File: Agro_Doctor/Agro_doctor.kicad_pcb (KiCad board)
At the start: 2 copper layers, 49 parts, among them J1 Bluetooth, J10 M2, J11 M3, J12 Power_Motor, J13 MS_Conn, J2 Bluetooth, J3 3STEPPER,1SERVO, J4 Bluetooth, J5 Encoders, Stepper1, J6 3 MPU, HUMIDITY, PH, J7 Power_Logic, J8 M1, J9 M4, SW1 SW_DIP_x01, U1 Motor_Driver, U10 Boost, U2 A4988_1, U3 A4988_2, U4 A4988_3, U5 A4988_4, U6 L298_M2,3, U7 L298_M4, U8 Buck, U9 STM32F407_Discovery

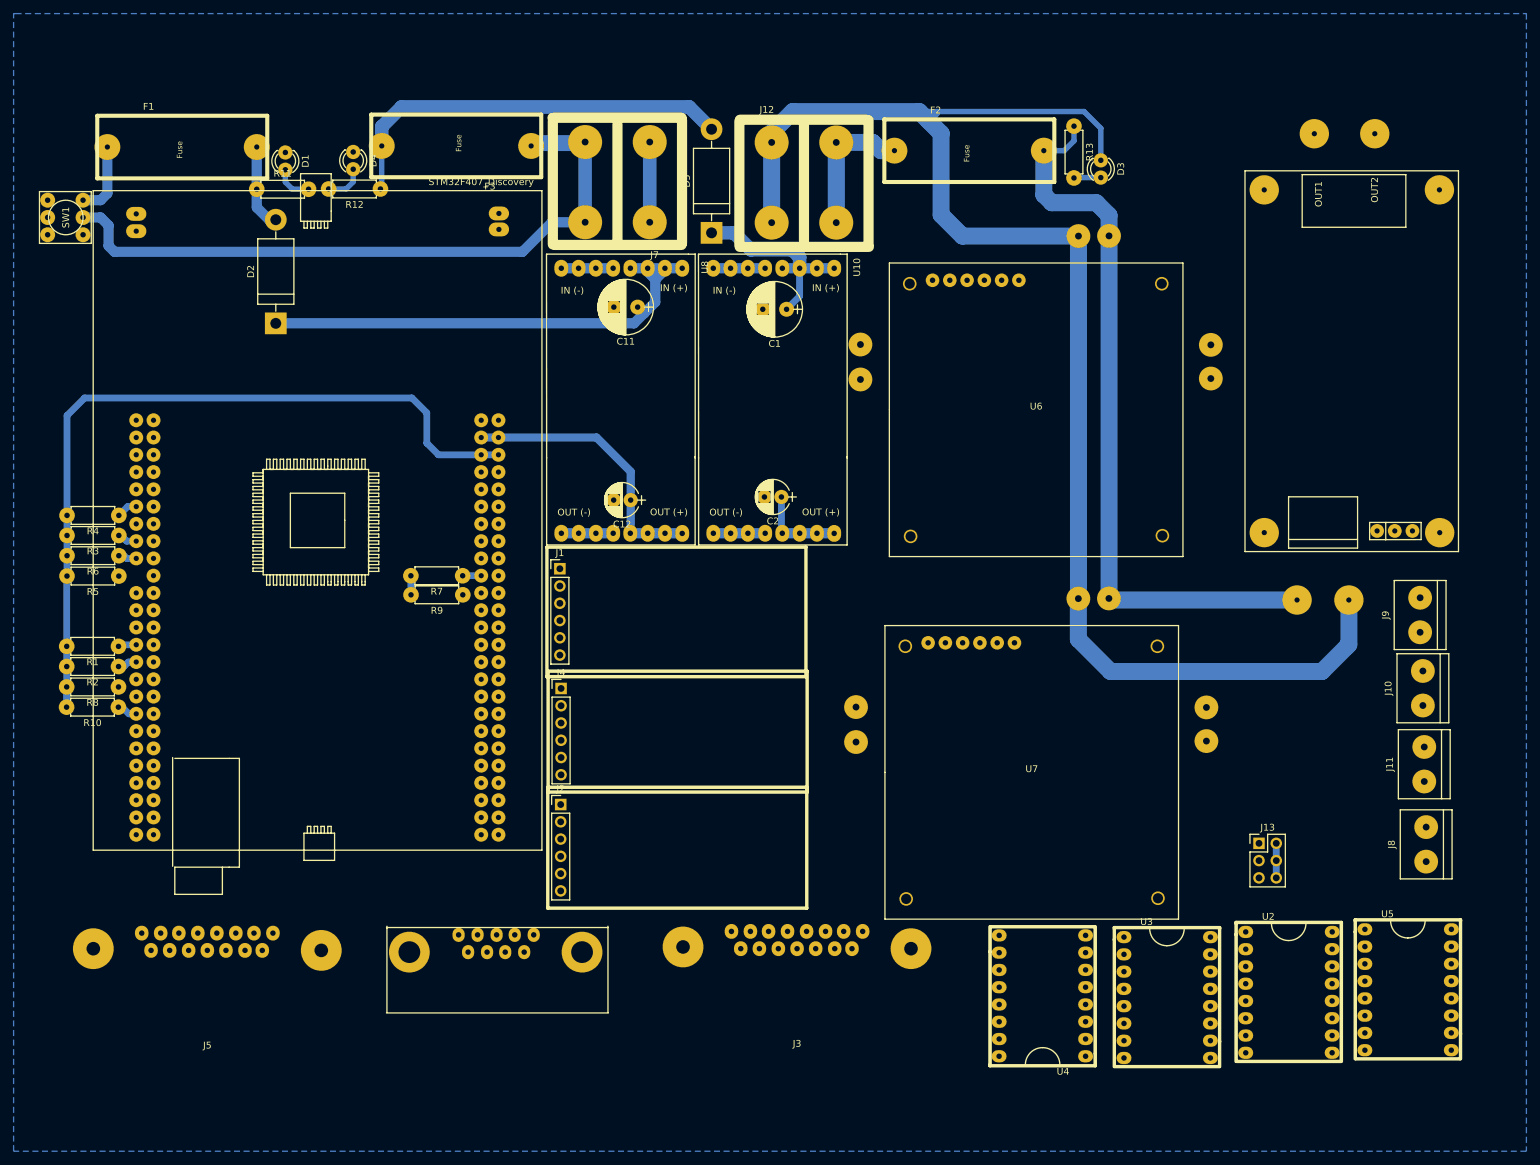
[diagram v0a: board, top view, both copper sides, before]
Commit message: added the minor project file
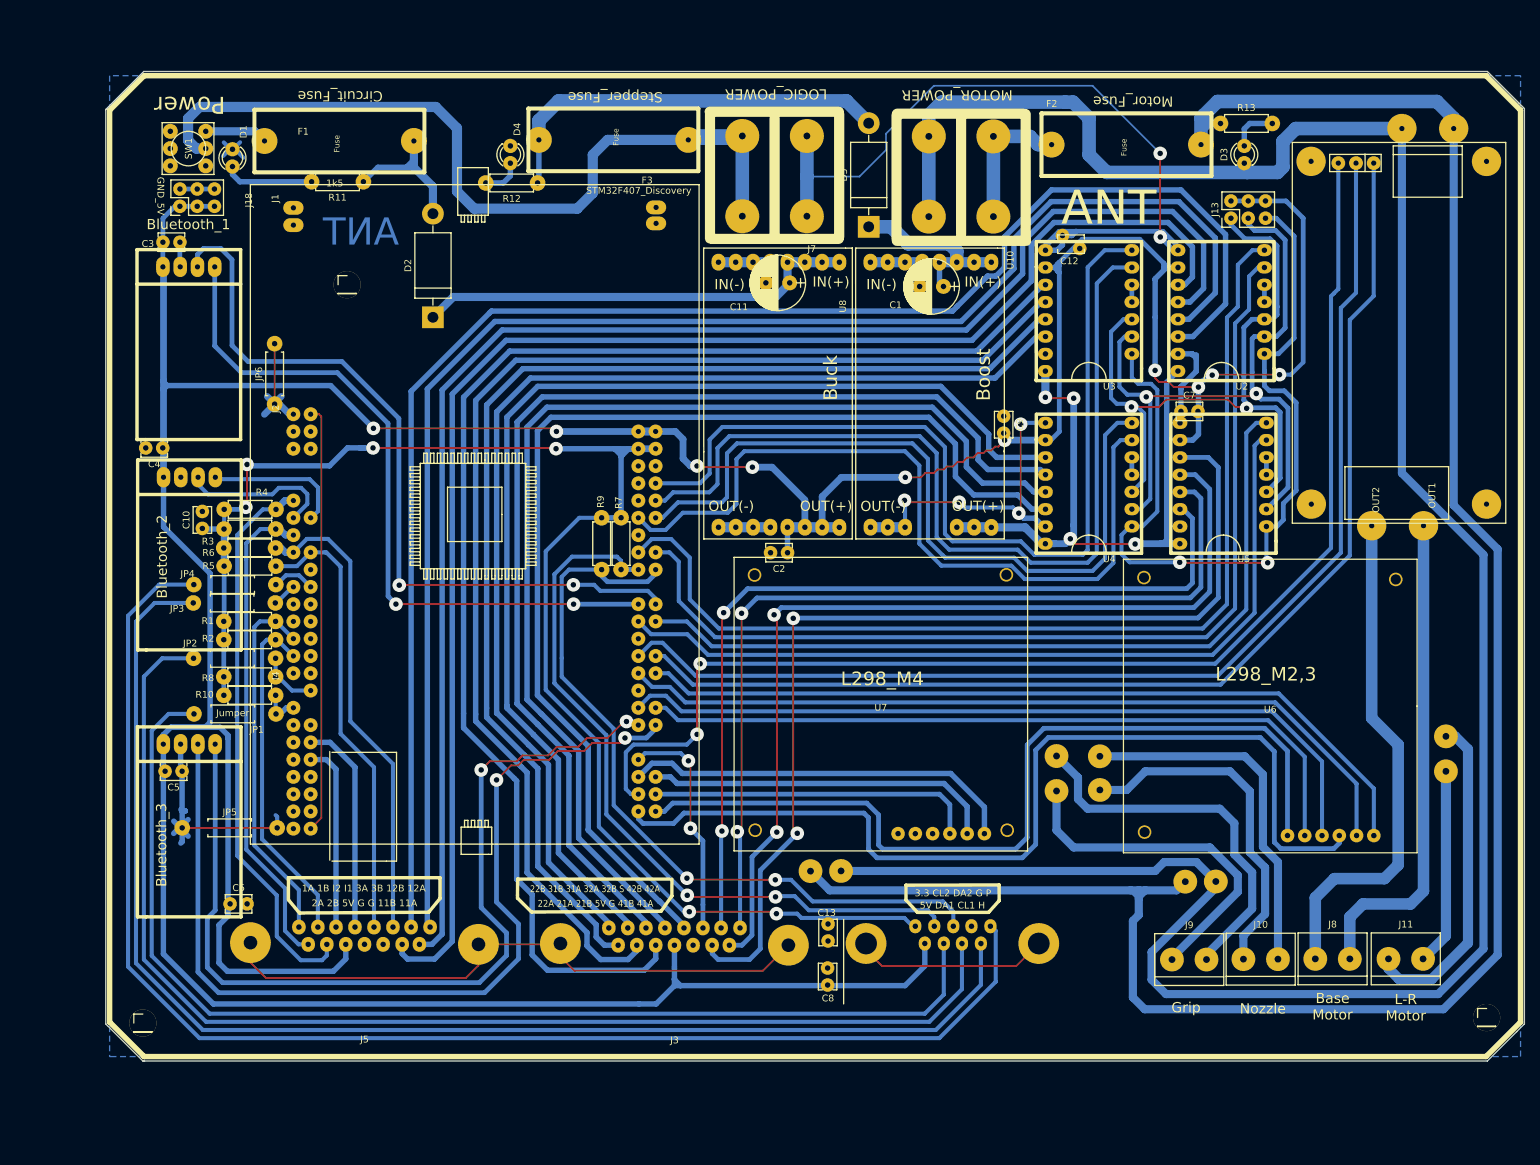
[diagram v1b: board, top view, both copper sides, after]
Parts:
- added C10: C, modFiles:Capacitor_Disc_Small, F.Cu at (51.3, 92.8)
- added C13: C, modFiles:Capacitor_Disc_Small, F.Cu at (143.4, 150.9)
- added C3: C, modFiles:Capacitor_Disc_Small, F.Cu at (48.0, 50.6)
- added C4: C, modFiles:Capacitor_Disc_Small, F.Cu at (45.5, 80.9)
- added C5: C, modFiles:Capacitor_Disc_Small, F.Cu at (48.4, 128.5)
- added C6: C, modFiles:Capacitor_Disc_Small, F.Cu at (55.4, 148.0)
- added C7: C, modFiles:Capacitor_Disc_Small, F.Cu at (195.3, 75.5)
- added C8: C, modFiles:Capacitor_Disc_Small, F.Cu at (143.3, 159.9)
- added C9: C, modFiles:Capacitor_Disc_Small, F.Cu at (169.2, 76.2)
- added J14: Conn_01x01, Pin_Headers:Pin_Header_Straight_1x01_Pitch2.54mm, F.Cu at (240.2, 164.7)
- added J15: Conn_01x01, Pin_Headers:Pin_Header_Straight_1x01_Pitch2.54mm, F.Cu at (72.6, 56.9)
- added J16: Conn_01x01, Pin_Headers:Pin_Header_Straight_1x01_Pitch2.54mm, F.Cu at (42.6, 165.5)
- added J18: GND_5V, Pin_Headers:Pin_Header_Straight_2x03_Pitch2.54mm, F.Cu at (48.0, 45.4)
- added JP1: Jumper, modFiles:Resistor_small, F.Cu at (59.6, 120.0)
- added JP2: Jumper, modFiles:Resistor_small, F.Cu at (59.6, 111.8)
- added JP3: Jumper, modFiles:Resistor_small, F.Cu at (59.5, 103.7)
- added JP4: Jumper, modFiles:Resistor_small, F.Cu at (59.6, 101.0)
- added JP5: Jumper, modFiles:Resistor_small, F.Cu at (51.6, 136.8)
- added JP6: Jumper, modFiles:Resistor_small, F.Cu at (62.0, 73.8)
- C12, C2: value 10uf -> C; footprint modFiles:Capacitor_10uF -> modFiles:Capacitor_Disc_Small
- J1: value Bluetooth -> Bluetooth_1; footprint Pin_Headers:Pin_Header_Straight_1x06_Pitch2.54mm -> modFiles:Bluetooth_horizontal
- J2: value Bluetooth -> Bluetooth_2; footprint Pin_Headers:Pin_Header_Straight_1x06_Pitch2.54mm -> modFiles:Bluetooth_horizontal
- J4: value Bluetooth -> Bluetooth_3; footprint Pin_Headers:Pin_Header_Straight_1x06_Pitch2.54mm -> modFiles:Bluetooth_horizontal
- R12: value R -> 1k5
- SW1: value SW_DIP_x01 -> Power
- moved J13 92.0 mm to (202.6, 47.1), turned to 90 degrees
- moved U3 83.3 mm to (189.4, 69.6), turned to 180 degrees
- moved U2 82.7 mm to (208.9, 69.6), turned to 180 degrees
- moved U4 75.7 mm to (189.4, 95.0)
- moved C12 73.8 mm to (177.9, 50.9), turned to 0 degrees
- moved J2 71.8 mm to (53.3, 82.7), turned to 270 degrees
- moved J1 69.1 mm to (53.2, 51.7), turned to 270 degrees
- moved J6 67.2 mm to (167.3, 151.3)
- moved J9 60.4 mm to (194.0, 156.2), turned to 0 degrees
- moved U5 57.9 mm to (209.1, 95.0), turned to 180 degrees
- moved U6 55.5 mm to (208.4, 118.9), turned to 0 degrees
- moved U1 52.6 mm to (229.0, 40.3), turned to 90 degrees
- moved J4 51.2 mm to (53.2, 121.9), turned to 270 degrees
- moved J10 45.7 mm to (204.5, 156.1), turned to 0 degrees
- moved J11 26.6 mm to (225.8, 156.1), turned to 0 degrees
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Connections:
- C12 pad 1: +5V -> GND
- C12 pad 2: GND -> +5V
- C2 pad 1: /18V -> +5V
- J13 pad 1: Net-(J13-Pad1) -> /MS3
- J13 pad 2: Net-(J13-Pad2) -> /MS2
- J13 pad 3: Net-(J13-Pad3) -> /MS1
- J3 pad 0: Net-(J3-Pad0) -> GND
- J3 pad 1: /S2_2B -> /S4_2A
- J3 pad 10: /S2_1B -> /S4_1B
- J3 pad 11: /S3_2A -> GND
- J3 pad 12: /S3_1B -> +5V
- J3 pad 13: /S4_2A -> /S2_1B
- J3 pad 14: /S4_1B -> /S2_1A
- J3 pad 15: /SERVO -> /S2_2A
- J3 pad 2: /S2_1A -> /S4_2B
- J3 pad 3: /S3_2B -> /SERVO
- J3 pad 4: /S3_1A -> /S3_2B
- J3 pad 5: /S4_2B -> /S3_2A
- J3 pad 6: /S4_1A -> /S3_1A
- J3 pad 7: GND -> /S3_1B
- J3 pad 8: +5V -> /S2_2B
- J3 pad 9: /S2_2A -> /S4_1A
- J5 pad 0: Net-(J5-Pad0) -> GND
- J5 pad 1: /S1_1B -> /S1_2A
- J5 pad 10: /S1_2B -> /S1_1B
- J5 pad 11: /E2_CHA -> GND
- J5 pad 12: /E1_CHB -> GND
- J5 pad 13: /E1_CHA -> +5V
- J5 pad 14: +5V -> /E2_CHB
- J5 pad 15: Net-(J5-Pad15) -> /E2_CHA
- J5 pad 2: /S1_2A -> /S1_2B
- J5 pad 5: /E2_CHB -> /INT1
- J5 pad 6: /INT1 -> /INT2
- J5 pad 7: GND -> /E1_CHB
- J5 pad 8: /INT2 -> /E1_CHA
- J6 pad 1: /I2C2_SDA -> Net-(J6-Pad1)
- J6 pad 2: /HUMIDITY -> GND
- J6 pad 3: /PH -> /I2C1_SDA
- J6 pad 4: /I2C2_SCL -> /I2C1_SCL
- J6 pad 6: /I2C1_SDA -> Net-(J6-Pad6)
- J6 pad 7: /I2C1_SCL -> Net-(J6-Pad7)
- J6 pad 8: GND -> Net-(J6-Pad8)
- U1 pad 1: Net-(U1-Pad1) -> Net-(J8-Pad2)
- U1 pad 2: Net-(U1-Pad2) -> Net-(J8-Pad1)
- U1 pad 3: Net-(U1-Pad3) -> /M1_PWM
- U1 pad 4: Net-(U1-Pad4) -> /M1_EN1
- U1 pad 5: Net-(U1-Pad5) -> /M1_EN2
- U2 pad 10: Net-(U2-Pad10) -> +5V
- U2 pad 11: Net-(U2-Pad11) -> /S1_1B
- U2 pad 12: Net-(U2-Pad12) -> /S1_1A
- U2 pad 13: Net-(U2-Pad13) -> /S1_2A
- U2 pad 14: Net-(U2-Pad14) -> /S1_2B
- U2 pad 15: Net-(U2-Pad15) -> GND
- U2 pad 16: Net-(U2-Pad16) -> /18V
- U2 pad 2: Net-(U2-Pad2) -> /MS1
- U2 pad 3: Net-(U2-Pad3) -> /MS2
- U2 pad 4: Net-(U2-Pad4) -> /MS3
- U2 pad 6: Net-(U2-Pad6) -> Net-(U2-Pad5)
- U2 pad 7: Net-(U2-Pad7) -> /S1_DIR
- U2 pad 8: Net-(U2-Pad8) -> /S1_STEP
- U2 pad 9: Net-(U2-Pad9) -> GND
- U3 pad 10: Net-(U3-Pad10) -> +5V
- U3 pad 11: Net-(U3-Pad11) -> /S2_1B
- U3 pad 12: Net-(U3-Pad12) -> /S2_1A
- U3 pad 13: Net-(U3-Pad13) -> /S2_2A
- U3 pad 14: Net-(U3-Pad14) -> /S2_2B
- U3 pad 15: Net-(U3-Pad15) -> GND
- U3 pad 16: Net-(U3-Pad16) -> /18V
- U3 pad 2: Net-(U3-Pad2) -> /MS1
- U3 pad 3: Net-(U3-Pad3) -> /MS2
- U3 pad 4: Net-(U3-Pad4) -> /MS3
- U3 pad 6: Net-(U3-Pad6) -> Net-(U3-Pad5)
- U3 pad 7: Net-(U3-Pad7) -> /S2_DIR
- U3 pad 8: Net-(U3-Pad8) -> /S2_STEP
- U3 pad 9: Net-(U3-Pad9) -> GND
- U4 pad 10: Net-(U4-Pad10) -> +5V
- U4 pad 11: Net-(U4-Pad11) -> /S3_1B
- U4 pad 12: Net-(U4-Pad12) -> /S3_1A
- U4 pad 13: Net-(U4-Pad13) -> /S3_2A
- U4 pad 14: Net-(U4-Pad14) -> /S3_2B
- U4 pad 15: Net-(U4-Pad15) -> GND
- U4 pad 16: Net-(U4-Pad16) -> /18V
- U4 pad 2: Net-(U4-Pad2) -> /MS1
- U4 pad 3: Net-(U4-Pad3) -> /MS2
- U4 pad 4: Net-(U4-Pad4) -> /MS3
- U4 pad 6: Net-(U4-Pad6) -> Net-(U4-Pad5)
- U4 pad 7: Net-(U4-Pad7) -> /S3_DIR
- U4 pad 8: Net-(U4-Pad8) -> /S3_STEP
- U4 pad 9: Net-(U4-Pad9) -> GND
- U5 pad 10: Net-(U5-Pad10) -> +5V
- U5 pad 11: Net-(U5-Pad11) -> /S4_1B
- U5 pad 12: Net-(U5-Pad12) -> /S4_1A
- U5 pad 13: Net-(U5-Pad13) -> /S4_2A
- U5 pad 14: Net-(U5-Pad14) -> /S4_2B
- U5 pad 15: Net-(U5-Pad15) -> GND
- U5 pad 16: Net-(U5-Pad16) -> /18V
- U5 pad 2: Net-(U5-Pad2) -> /MS1
- U5 pad 3: Net-(U5-Pad3) -> /MS2
- U5 pad 4: Net-(U5-Pad4) -> /MS3
- U5 pad 6: Net-(U5-Pad6) -> Net-(U5-Pad5)
- U5 pad 7: Net-(U5-Pad7) -> /S4_DIR
- U5 pad 8: Net-(U5-Pad8) -> /S4_STEP
- U5 pad 9: Net-(U5-Pad9) -> GND
- U6 pad 10: Net-(U6-Pad10) -> Net-(J10-Pad1)
- U6 pad 11: Net-(U6-Pad11) -> Net-(J11-Pad1)
- U6 pad 12: Net-(U6-Pad12) -> Net-(J11-Pad2)
- U6 pad 3: Net-(U6-Pad3) -> /M2_PWM
- U6 pad 4: Net-(U6-Pad4) -> /M2_EN1
- U6 pad 5: Net-(U6-Pad5) -> /M2_EN2
- U6 pad 6: Net-(U6-Pad6) -> /M3_PWM
- U6 pad 7: Net-(U6-Pad7) -> /M3_EN1
- U6 pad 8: Net-(U6-Pad8) -> /M3_EN2
- U6 pad 9: Net-(U6-Pad9) -> Net-(J10-Pad2)
- U7 pad 11: Net-(U7-Pad11) -> Net-(J9-Pad2)
- U7 pad 12: Net-(U7-Pad12) -> Net-(J9-Pad1)
- U7 pad 6: Net-(U7-Pad6) -> /M4_PWM
- U7 pad 7: Net-(U7-Pad7) -> /M4_EN1
- U7 pad 8: Net-(U7-Pad8) -> /M4_EN2
- U9 pad 21: Net-(U9-Pad21) -> /HUMIDITY
- U9 pad 22: Net-(U9-Pad22) -> /PH
- U9 pad 40: Net-(U9-Pad40) -> /INT1
- U9 pad 42: Net-(U9-Pad42) -> /INT2
- U9 pad 60: Net-(U9-Pad60) -> /S2_STEP
- U9 pad 62: Net-(U9-Pad62) -> /S2_DIR
- U9 pad 63: Net-(U9-Pad63) -> /S3_DIR
- U9 pad 64: Net-(U9-Pad64) -> /S3_STEP
- U9 pad 67: Net-(U9-Pad67) -> /S1_STEP
- U9 pad 68: Net-(U9-Pad68) -> /S1_DIR
- U9 pad 75: Net-(U9-Pad75) -> /S4_DIR
- U9 pad 76: Net-(U9-Pad76) -> /S4_STEP
- U9 pad 79: Net-(U9-Pad79) -> /M1_EN1
- U9 pad 80: Net-(U9-Pad80) -> /M1_EN2
- U9 pad 81: Net-(U9-Pad81) -> /M3_EN1
- U9 pad 82: Net-(U9-Pad82) -> /M3_EN2
- U9 pad 85: Net-(U9-Pad85) -> /M2_EN2
- U9 pad 86: Net-(U9-Pad86) -> /M2_EN1
- U9 pad 93: Net-(U9-Pad93) -> /M4_EN2
- U9 pad 94: Net-(U9-Pad94) -> /M4_EN1
- U9 pad 95: /M3_PWM -> /M1_PWM
- U9 pad 97: Net-(U9-Pad97) -> /M3_PWM
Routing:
- net +5V: track 45.9 -> 622.8 mm, vias 0 -> 10
- net GND: track 42.3 -> 518.5 mm, vias 0 -> 6
- net /S1_2B: track 0.00 -> 235.4 mm
- net /S1_2A: track 0.00 -> 226.5 mm
- net /S1_1A: track 0.00 -> 222.8 mm
- net /S1_1B: track 0.00 -> 221.6 mm
- net Net-(J6-Pad1): track 0.00 -> 207.2 mm
- net /12VMOT: track 108.6 -> 313.6 mm
- net /S2_1B: track 0.00 -> 200.4 mm
- net Net-(J6-Pad6): track 0.00 -> 197.0 mm
- net /M1_PWM: track 0.00 -> 186.6 mm, vias 0 -> 2
- net /S2_1A: track 0.00 -> 186.3 mm
- net Net-(J6-Pad7): track 0.00 -> 182.9 mm
- net /S2_2A: track 0.00 -> 176.1 mm
- net /M1_EN1: track 0.00 -> 171.9 mm
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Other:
- board outline added: 208.7 x 145.5 mm
- board text added: "1A 1B I2 I1 3A 3B 12B 12A"
- board text added: "22A 21A 21B 5V G 41B 41A"
- board text added: "22B 31B 31A 32A 32B S 42B 42A"
- board text added: "2A 2B 5V G G 11B 11A"
- board text added: "3.3 CL2 DA2 G P"
- board text added: "5V DA1 CL1 H"
- board text added: "ANT"
- board text added: "Base Motor"
- board text added: "Circuit_Fuse"
- board text added: "GND_5V"
- board text added: "Grip"
- board text added: "L-R Motor"
- board text added: "LOGIC_POWER"
- board text added: "MOTOR_POWER"
- board text added: "Motor_Fuse"
- board text added: "Nozzle"
- board text added: "Power"
- board text added: "Stepper_Fuse"
